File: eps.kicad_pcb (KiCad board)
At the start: 4 copper layers, 95.9 x 90.2 mm, 134 parts, among them J1 CONN_01X05, J2 CONN_01X05, J3 CONN_01X05, J4 CONN_01X05, J5 +BATT, J6 -BATT, J7 PROGRAMMING PORT, J8 H_EPS, J9 DEBUG, Q1 BSC026NE2LS5, Q2 BSC026NE2LS5, Q3 BSC026NE2LS5, Q4 BSC026NE2LS5, Q5 BSC026NE2LS5, Q6 BSC026NE2LS5, SW1 SW_RST, U1 ATMEGA32M1-MU, U10 ADS7952, U11 TPS630250, U12 bq297xx, U13 INA214, U14 INA214, U15 TPS630250, U16 TPS61088, U17 TPS61088, U18 ADS7952, U19 INA214, U2 INA214, U20 INA214, U21 INA214, U3 INA214, U4 INA214, U5 INA214, U6 ADA4891-4, U7 ADA4891-4, U8 SN65HVD230, U9 SST25VF016B, Y1 8MHz

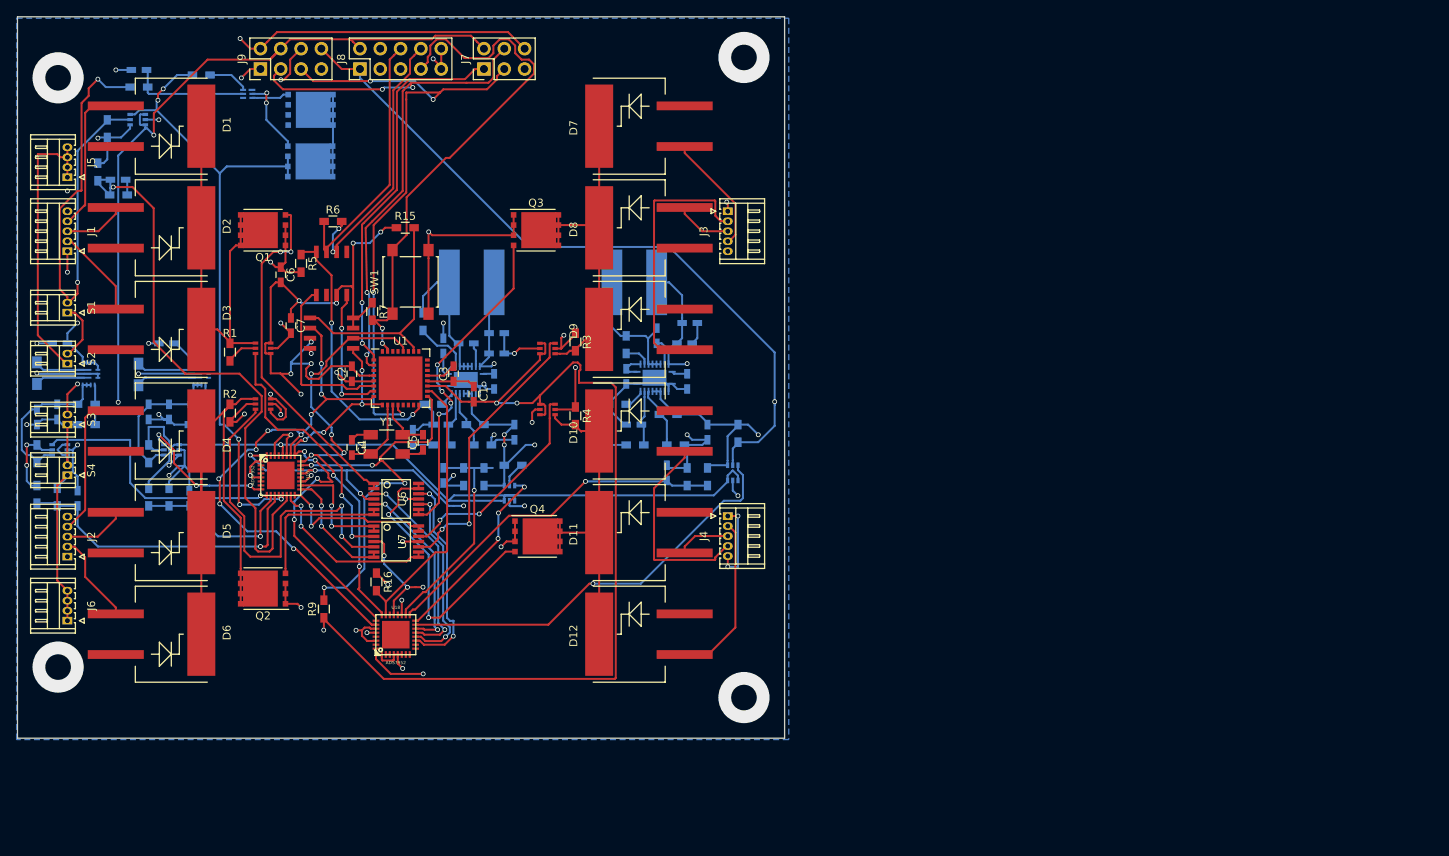
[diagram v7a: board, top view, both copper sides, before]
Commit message: Added REF5025 for 2.5V reference for ADCs
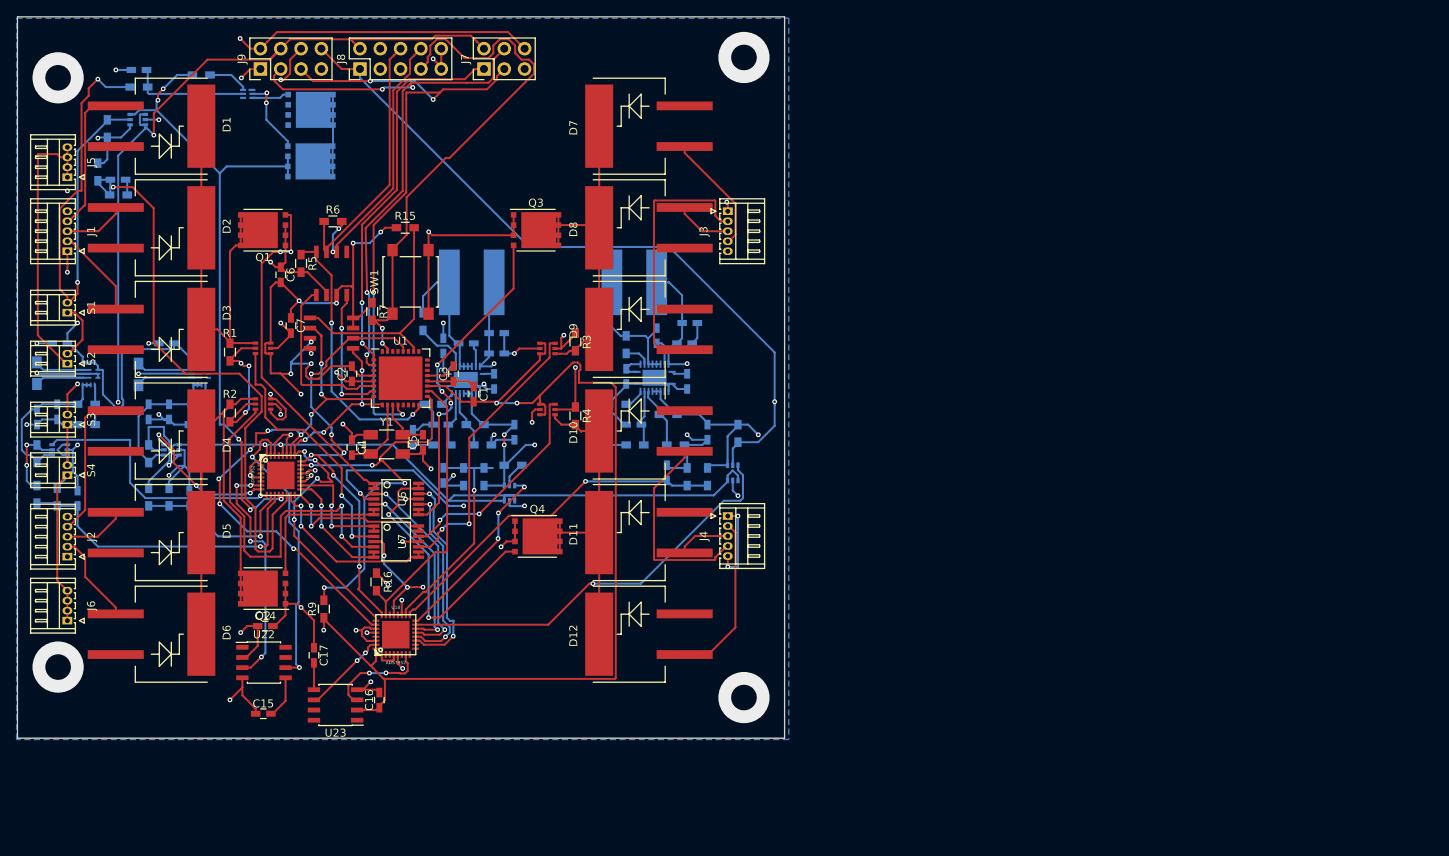
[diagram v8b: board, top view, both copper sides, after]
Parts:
- added C14: 10µ, Capacitors_SMD:C_0603_HandSoldering, F.Cu at (131.1, 126.0)
- added C15: 1µ, Capacitors_SMD:C_0603_HandSoldering, F.Cu at (130.8, 136.9)
- added C16: 10µ, Capacitors_SMD:C_0603_HandSoldering, F.Cu at (145.3, 135.2)
- added C17: 1µ, Capacitors_SMD:C_0603_HandSoldering, F.Cu at (137.2, 129.6)
- added G***: LOGO, eps-ssm:utat-logo, B.Cu at (170.3, 126.6)
- added U22: REF5025, Housings_SOIC:SOIC-8_3.9x4.9mm_Pitch1.27mm, F.Cu at (130.9, 130.5)
- added U23: REF5025, Housings_SOIC:SOIC-8_3.9x4.9mm_Pitch1.27mm, F.Cu at (139.9, 135.8)
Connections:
- U10 pad 21: +5V -> +3V3
- U10 pad 22: Net-(U10-Pad22) -> GND
- U10 pad 31: Net-(U10-Pad31) -> /2V5A
- U10 pad 32: +5V -> +3V3
- U10 pad 7: Net-(U10-Pad7) -> /TEMPA
- U18 pad 21: +5V -> +3V3
- U18 pad 22: Net-(U18-Pad22) -> GND
- U18 pad 31: Net-(U18-Pad31) -> /2V5B
- U18 pad 32: +5V -> +3V3
- U18 pad 7: Net-(U18-Pad7) -> /TEMPB
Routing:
- net /2V5A: track 0.00 -> 36.2 mm, vias 0 -> 2
- net +5V: track 155.3 -> 119.9 mm, vias 9 -> 4
- net GND: track 295.6 -> 327.1 mm, vias 52 -> 56
- net +3V3: track 422.4 -> 453.4 mm, vias 20 -> 25
- net +PACK: track 84.9 -> 115.0 mm, vias 8 -> 10
- net /TEMPA: track 0.00 -> 30.0 mm, vias 0 -> 4
- net /TEMPB: track 0.00 -> 12.9 mm, vias 0 -> 2
- net /2V5B: track 0.00 -> 10.8 mm, vias 0 -> 2
- net Net-(C15-Pad2): track 0.00 -> 5.38 mm
- net Net-(C17-Pad2): track 0.00 -> 3.35 mm
- net /3V3IOUT2: track 18.1 -> 18.6 mm
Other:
- board text added: "EPS MAIN 6.0 DESIGNED BY MITCHELL AU"
